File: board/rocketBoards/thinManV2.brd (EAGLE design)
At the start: 45 x 18 mm, 48 parts, among them J1 47346-0001

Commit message: thinManV2 changes
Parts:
- removed LED1: (no value), adafruit:CHIPLED_0603
- removed R10, R7, R8: (no value), ELL-i-Passives:R0402
- removed S1: SWITCH-MOMENTARY-2-SMD-1101NE, SparkFun-Electromechanical:TACTILE-SWITCH-1101NE
- removed S4: DPDT, SparkFun-Electromechanical:AYZ0202
- removed U$3: MICROSD-CD, Sensors:MOLEX_SD-47352-101
- added C2: 10uF, ELL-i-Passives:C0402
- added C4, C5: .1uF, ELL-i-Passives:C0402
- added D1, D2: (no value), SparkFun-LED:WS2812B
- added HIGHG: LPS331AP, Sensors:LGA-16-3X3X1
- added R5: (no value), ELL-i-Passives:R0402
- added S2: (no value), SparkFun-Electromechanical:SWITCH-SPST-SMD-A
- added U$1: RN4020, bluetooth:RN4020
- added U$7: S25FL127S, SparkFun-DigitalIC:SO08
- JP2: value (none) -> M02JST-PTH-VERT; device SparkFun-Connectors:1X04-1.5MM_JST -> SparkFun-Connectors:JST-2-PTH-VERT
- moved JP2 39.0 mm to (36.5, 5.17), turned to 270 degrees
- moved R2 26.5 mm to (40.6, 11.0)
- moved R3 24.9 mm to (39.1, 9.72)
- moved JP3 24.8 mm to (44.1, 4.42), turned to 270 degrees
- moved JP6 22.4 mm to (23.3, 16.4), flipped to the bottom, turned to 0 degrees
- moved LED2 21.9 mm to (38.4, 0.93)
- moved C22 21.6 mm to (30.6, 1.38)
- moved C26 21.6 mm to (31.9, 1.38)
- moved C27 21.6 mm to (33.1, 1.38)
- moved C30 21.6 mm to (29.4, 1.38)
- moved J1 21.1 mm to (32.0, 17.0)
- moved C14 20.1 mm to (28.0, 1.38), turned to 270 degrees
- moved R9 18.8 mm to (37.9, 2.50)
- moved C8 17.9 mm to (26.8, 1.38), turned to 270 degrees
- moved U$5 17.4 mm to (39.5, 14.9), turned to 135 degrees
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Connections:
- removed net BARO_INT2: U1.33
- removed net HIGHG_INT2: U1.36
- removed net INT2_A/G: U1.42
- removed net N$16: R7.1, U$3.1
- removed net N$19: S1.1, U1.26
- removed net N$21: R10.2, U$3.8
- new net N$6: D1.2, D2.4
- new net PIXEL: D1.4, U1.30
- new net SSP1_RST: U$7.7
- net 3.3V: now also C2.1, C4.1, C5.1, D1.1, D2.1, HIGHG.1, HIGHG.14, HIGHG.15, HIGHG.8, R5.2, U$7.8; no longer JP2.1, R10.1, R7.2, S4.6, U$3.4
- net GND: now also C2.2, C4.2, C5.2, D1.3, D2.3, HIGHG.10, HIGHG.12, HIGHG.13, HIGHG.16, HIGHG.5, HIGHG.7, JP2.2; no longer JP2.3, R8.1, S1.2, S4.4, U$3.6, U$3.G1, U$3.G2, U$3.G3, U$3.G4
- net HIGHG_INT1: now also HIGHG.11; no longer U1.32
- net I2C0_SCL: now also HIGHG.4
- net I2C0_SDA: now also HIGHG.6
- net LED_PIN2: no longer LED1.A
- net N$20: now also S2.1; no longer S4.1
- net N$4: now also R5.1, U$7.3; no longer LED1.C, R8.2
- net PIO0_1: now also JP2.1; no longer S4.5
- net SD_CD: no longer U$3.9
- net SSP1_MISO: now also U$7.2; no longer U$3.7
- net SSP1_MOSI: now also U$7.5; no longer U$3.3
- net SSP1_SCK: now also U$7.6; no longer U$3.5
- net SSP1_SSEL: now also U$7.1; no longer U$3.2
- net USB_VBUS: now also S2.3; no longer S4.3
- net VBUS: now also S2.2; no longer JP2.4, S4.2
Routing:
- net GND: track 199.8 -> 0.00 mm, vias 11 -> 0
- net 3.3V: track 148.1 -> 0.00 mm, vias 5 -> 0
- net I2C0_SCL: track 75.2 -> 0.00 mm, vias 4 -> 0
- net VBUS: track 40.9 -> 0.00 mm, vias 1 -> 0
- net I2C1_SCL: track 38.2 -> 0.00 mm, vias 4 -> 0
- net I2C1_SDA: track 35.4 -> 0.00 mm, vias 4 -> 0
- net I2C0_SDA: track 32.1 -> 0.00 mm, vias 4 -> 0
- net SSP1_MISO: track 31.7 -> 0.00 mm, vias 5 -> 0
- net N$1: track 30.9 -> 0.00 mm, vias 2 -> 0
- net DRDY_M: track 29.3 -> 0.00 mm, vias 4 -> 0
- net INT1_A/G: track 26.0 -> 0.00 mm, vias 2 -> 0
- net PIO0_1: track 25.2 -> 0.00 mm, vias 2 -> 0
- net SSP1_MOSI: track 22.3 -> 0.00 mm, vias 1 -> 0
- net SSP1_SCK: track 22.2 -> 0.00 mm, vias 3 -> 0
- net N$19: track 20.7 -> 0.00 mm, vias 2 -> 0
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- removed copper zone on layer 1, net GND
- removed copper zone on layer 16, net GND

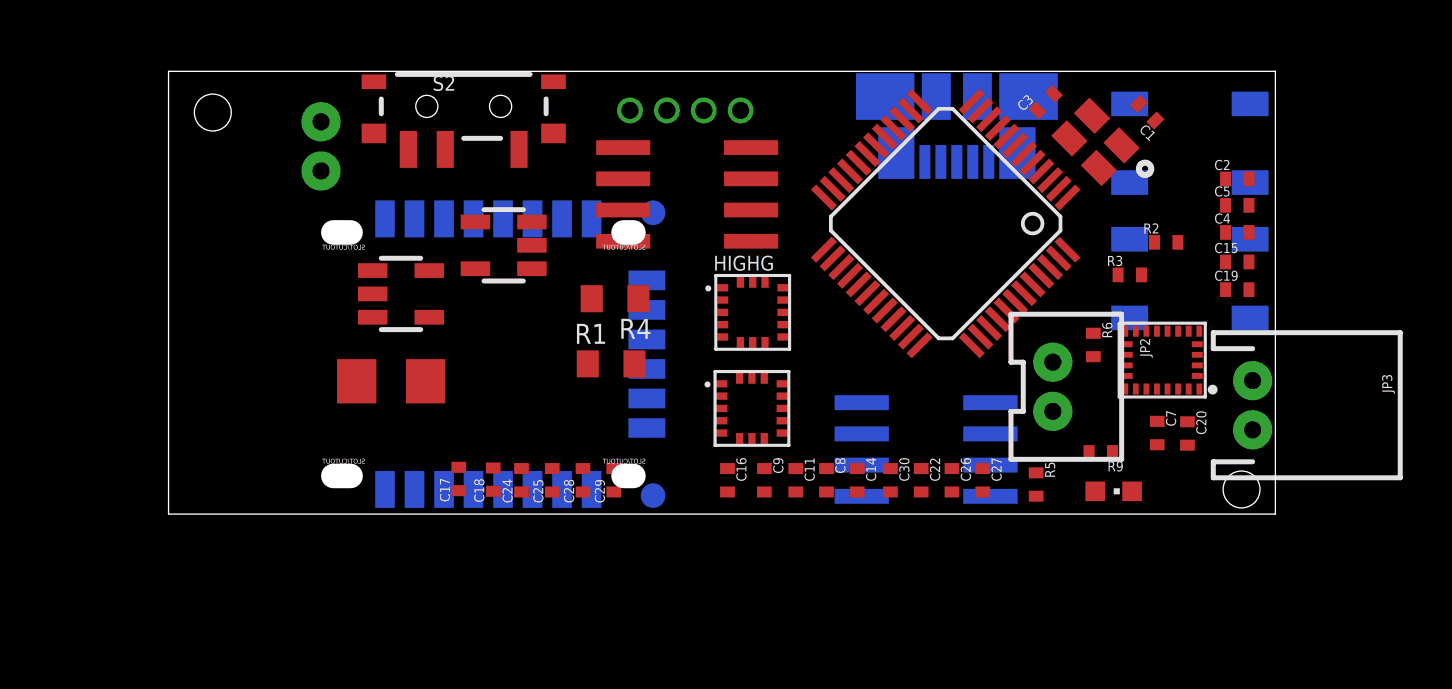
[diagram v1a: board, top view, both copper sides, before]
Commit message: updated thinManV2 and lipoWing to use 0603 parts
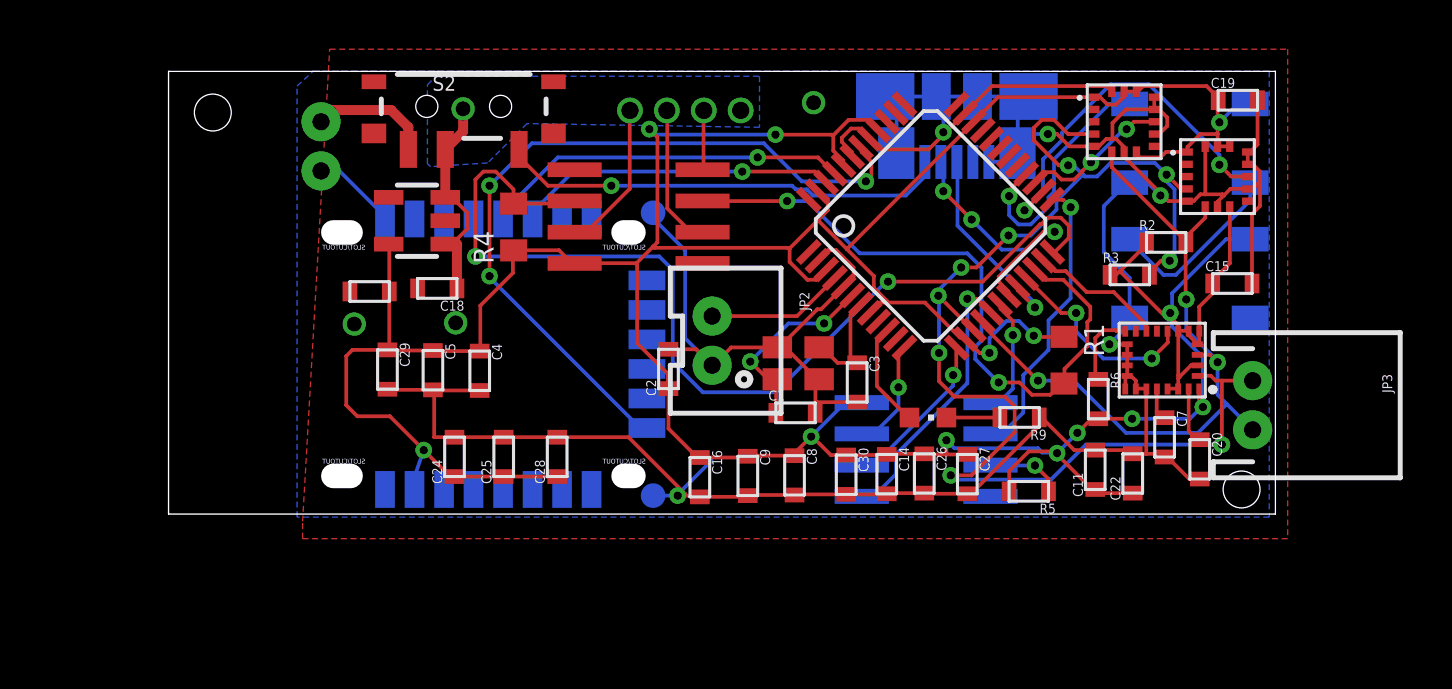
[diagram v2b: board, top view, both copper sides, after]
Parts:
- removed C17: 1uF, ELL-i-Passives:C0402
- removed HIGHG: LPS331AP, Sensors:LGA-16-3X3X1
- removed U$2: LDK220M33R, Sensors:SOT23-5
- added BARO1: LPS331AP, Sensors:LGA-16-3X3X1
- C1, C11, C14, C15, C16, C18, C19, C2, C20, C22, C24, C25, C26, C27, C28, C29, C3, C30, C4, C5, C7, C8, C9: device ELL-i-Passives:C0402 -> ELL-i-Passives:C0603
- C21: device ELL-i-Passives:C1206 -> ELL-i-Passives:C0603
- R2, R3, R5, R6, R9: device ELL-i-Passives:R0402 -> ELL-i-Passives:R0603
- moved C5 33.4 mm to (10.8, 5.85), turned to 270 degrees
- moved C4 31.3 mm to (12.7, 5.83), turned to 270 degrees
- moved C2 24.4 mm to (20.3, 5.90), turned to 90 degrees
- moved BARO 21.1 mm to (41.1, 12.2)
- moved C1 18.8 mm to (25.5, 4.12), turned to 0 degrees
- moved R1 18.4 mm to (36.4, 6.25), turned to 270 degrees
- moved U$5 18.3 mm to (24.1, 4.98), turned to 0 degrees
- moved JP2 14.0 mm to (22.6, 7.05)
- moved C3 13.7 mm to (28.0, 5.35), turned to 270 degrees
- moved C11 12.2 mm to (37.7, 1.80), turned to 90 degrees
- moved C29 10.2 mm to (8.90, 5.88), turned to 270 degrees
- moved C22 8.60 mm to (39.2, 1.65), turned to 90 degrees
- moved LED2 8.12 mm to (30.9, 3.92)
- moved C18 8.10 mm to (10.9, 9.18), turned to 180 degrees
- moved C19 7.70 mm to (43.5, 16.8)
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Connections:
- removed net LED_PIN2: U1.11
- removed net N$18: U1.25
- removed net N$22: U1.12
- removed net SD_CD: U1.9
- new net BLE_RX: U$1.5, U1.45
- new net BLE_TX: U$1.6, U1.46
- new net BLE_WAKE: U$1.15, U1.42
- net 3.3V: now also BARO1.1, BARO1.14, BARO1.15, BARO1.8, R3.1, U$1.23; no longer HIGHG.1, HIGHG.14, HIGHG.15, HIGHG.8, U$2.5
- net BARO_INT1: now also U1.26; no longer U1.37
- net DRDY_M: now also U1.21; no longer U1.46
- net GND: now also BARO1.10, BARO1.12, BARO1.13, BARO1.16, BARO1.5, BARO1.7, U$1.1, U$1.16, U$1.24, U$1.9; no longer C17.2, HIGHG.10, HIGHG.12, HIGHG.13, HIGHG.16, HIGHG.5, HIGHG.7, U$2.2
- net HIGHG_INT1: now also BARO1.11, U1.27; no longer HIGHG.11
- net I2C0_SCL: now also BARO1.4; no longer HIGHG.4
- net I2C0_SDA: now also BARO1.6; no longer HIGHG.6
- net INT1_A/G: now also U1.23; no longer U1.45
- net PIXEL: now also U1.28; no longer U1.30
- net SSP1_MISO: now also U1.25; no longer U1.29
- net SSP1_RST: now also U1.12
- net SSP1_SSEL: now also U1.18; no longer U1.38
- net VBUS: no longer C17.1, U$2.1, U$2.3
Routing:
- net 3.3V: track 0.00 -> 172.0 mm, vias 0 -> 13
- net GND: track 0.00 -> 146.0 mm, vias 0 -> 8
- net I2C0_SCL: track 0.00 -> 54.0 mm, vias 0 -> 9
- net I2C1_SCL: track 0.00 -> 41.3 mm, vias 0 -> 2
- net BLE_WAKE: track 0.00 -> 31.0 mm, vias 0 -> 3
- net I2C0_SDA: track 0.00 -> 28.8 mm, vias 0 -> 3
- net I2C1_SDA: track 0.00 -> 27.1 mm, vias 0 -> 2
- net USB_VBUS: track 0.00 -> 18.4 mm, vias 0 -> 1
- net BARO_INT1: track 0.00 -> 15.0 mm, vias 0 -> 2
- net BLE_RX: track 0.00 -> 15.0 mm, vias 0 -> 1
- net BLE_TX: track 0.00 -> 13.1 mm, vias 0 -> 1
- net SSP1_MISO: track 0.00 -> 11.7 mm, vias 0 -> 1
- net SSP1_MOSI: track 0.00 -> 11.3 mm, vias 0 -> 1
- net N$17: track 0.00 -> 11.0 mm, vias 0 -> 3
- net PIXEL: track 0.00 -> 10.1 mm, vias 0 -> 1
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- added copper zone on layer 1, net GND
- added copper zone on layer 16, net GND
- added copper zone on layer 16, net VBUS

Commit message: boards shipped
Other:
- board text added: "This Side Up"
- board text added: "teamRocket"
- board text added: "thinManV2"
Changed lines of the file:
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@@
 <hole x="43.625" y="1" drill="1.5"/>
 <hole x="1.8" y="16.325" drill="1.5"/>
+<text x="2.075" y="4.55" size="1.4224" layer="21" rot="R90">thinManV2</text>
+<text x="3.3" y="7.775" size="0.6096" layer="21" rot="R90">teamRocket</text>
+<text x="4.775" y="5.925" size="0.8128" layer="21" rot="R90">This Side Up</text>
+<wire x1="4.425" y1="16.525" x2="4.425" y2="15.275" width="0.25" layer="21"/>
 </plain>
 <attributes>
